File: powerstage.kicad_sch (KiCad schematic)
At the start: 0 parts

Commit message: Added driver and powerstage
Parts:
- added C10, C11, C12: 470uF, Capacitor_THT:CP_Radial_D17.0mm_P7.50mm, symbol Device:C_Polarized
- added C13, C14: 1uF, Capacitor_SMD:C_0805_2012Metric_Pad1.18x1.45mm_HandSolder, symbol Device:C
- added D10, D5, D6, D7, D8, D9: D_Zener, symbol Device:D_Zener
- added D2: B120-E3, Diode_SMD:D_SOD-128, symbol Diode:B120-E3
- added F1: Fuse, Fuse:Fuseholder_Cylinder-6.3x32mm_Schurter_0031-8002_Horizontal_Open, symbol Device:Fuse
- added H1: V_RAW, MountingHole:MountingHole_5.3mm_M5_Pad_Via, symbol Mechanical:MountingHole_Pad
- added H2: GND, MountingHole:MountingHole_5.3mm_M5_Pad_Via, symbol Mechanical:MountingHole_Pad
- added H3: PAD_A, MountingHole:MountingHole_5.3mm_M5_Pad_Via, symbol Mechanical:MountingHole_Pad
- added H4: PAD_B, MountingHole:MountingHole_5.3mm_M5_Pad_Via, symbol Mechanical:MountingHole_Pad
- added H5: PAD_C, MountingHole:MountingHole_5.3mm_M5_Pad_Via, symbol Mechanical:MountingHole_Pad
- added Q1, Q2, Q3, Q4, Q5, Q6: BSP89, Package_TO_SOT_THT:TO-220-3_Horizontal_TabDown, symbol Transistor_FET:BSP89
- added R10: 2k2, Resistor_SMD:R_1206_3216Metric, symbol Device:R
- added R11, R12, R13, R14, R15, R16, R17, R18, R19, R20, R21, R22: 10k, Resistor_SMD:R_1206_3216Metric, symbol Device:R
- added R9: 47k, Resistor_SMD:R_1206_3216Metric, symbol Device:R
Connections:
- new net: Q3.1 (G), R13.2, R19.2
- new net: Q2.1 (G), R12.2, R18.2
- new net: Q1.1 (G), R11.2, R17.2
- new net: F1.1, H1.1
- new net: Q6.1 (G), R16.2, R22.2
- new net: Q4.1 (G), R14.2, R20.2
- new net: Q5.1 (G), R15.2, R21.2
- new net COM_A: D5.2 (A), H3.1, Q1.3 (S), Q2.2 (D), R17.1
- new net COM_B: D7.2 (A), H4.1, Q3.3 (S), Q4.2 (D), R19.1
- new net COM_C: D9.2 (A), H5.1, Q5.3 (S), Q6.2 (D), R21.1
- new net DRV_AH: D5.1 (K), R11.1
- new net DRV_AL: D6.1 (K), R12.1
- new net DRV_BH: D7.1 (K), R13.1
- new net DRV_BL: D8.1 (K), R14.1
- new net DRV_CH: D9.1 (K), R15.1
- new net DRV_CL: D10.1 (K), R16.1
- new net GND: C10.2, C11.2, C12.2, C13.2, C14.2, D10.2 (A), D2.2 (A), D6.2 (A), D8.2 (A), H2.1, Q2.3 (S), Q4.3 (S), Q6.3 (S), R10.2, R18.1, R20.1, R22.1
- new net VSENSE: R10.1, R9.2
- new net V_RAW: C10.1, C11.1, C12.1, C13.1, C14.1, D2.1 (K), F1.2, Q1.2 (D), Q3.2 (D), Q5.2 (D), R9.1

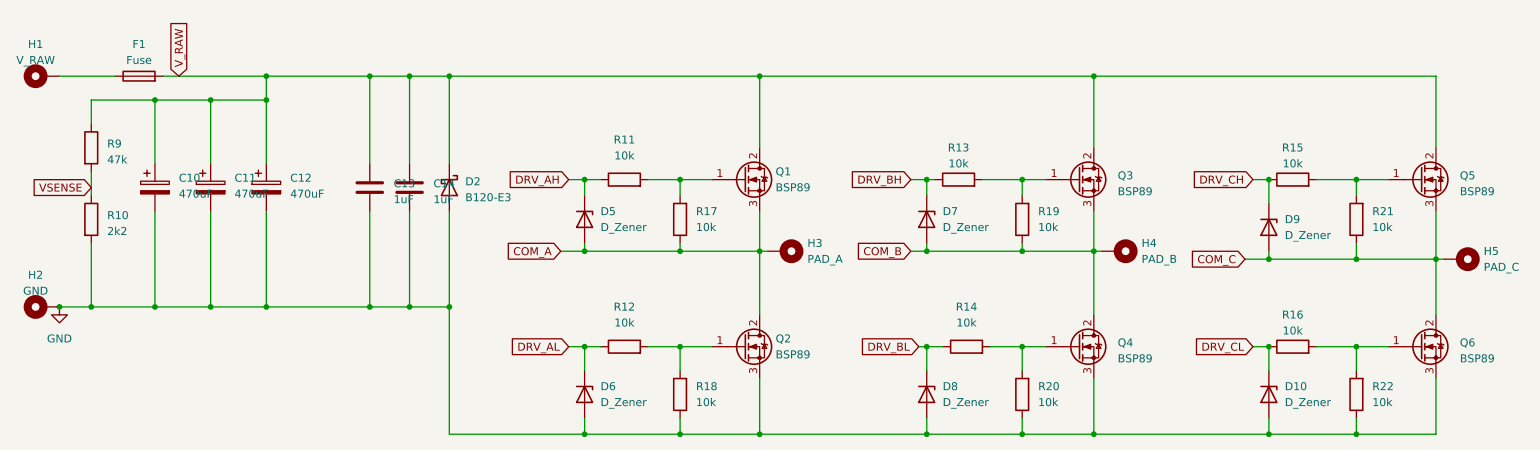
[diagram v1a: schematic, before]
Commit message: initial pcb placment, some components needs to be replaced by smd
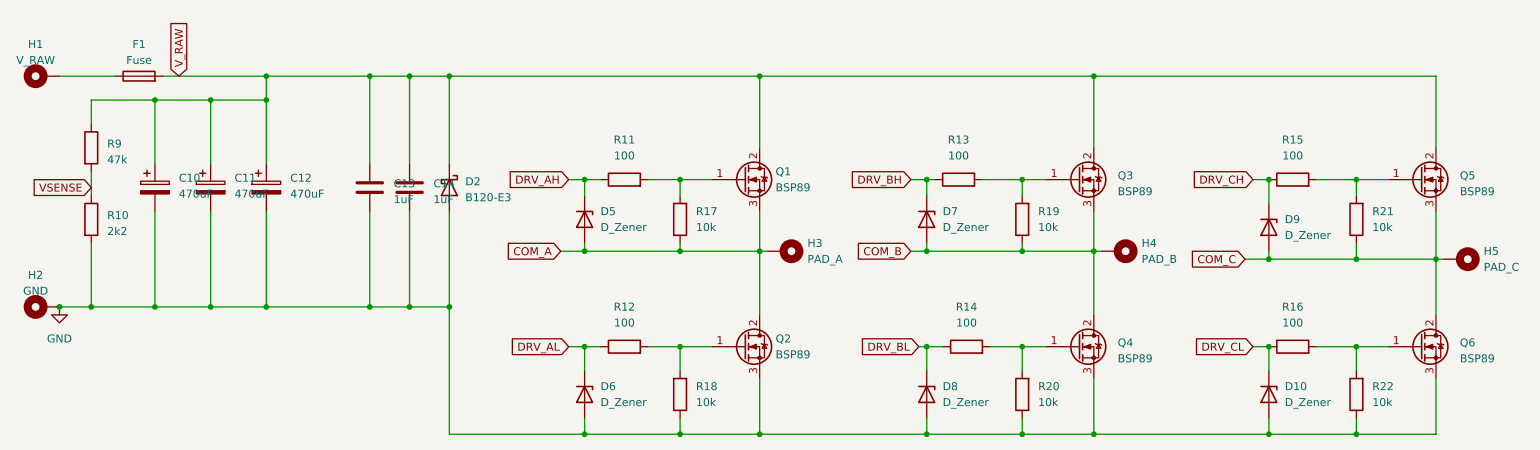
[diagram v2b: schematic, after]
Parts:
- C13, C14: footprint Capacitor_SMD:C_0805_2012Metric_Pad1.18x1.45mm_HandSolder -> Capacitor_THT:CP_Radial_Tantal_D5.5mm_P5.00mm
- D10, D5, D6, D7, D8, D9: footprint (none) -> Diode_THT:D_5W_P12.70mm_Horizontal
- D2: footprint Diode_SMD:D_SOD-128 -> Diode_THT:D_A-405_P10.16mm_Horizontal
- F1: footprint Fuse:Fuseholder_Cylinder-6.3x32mm_Schurter_0031-8002_Horizontal_Open -> Fuse:Fuse_Blade_ATO_directSolder
- H1, H2, H3, H4, H5: footprint MountingHole:MountingHole_5.3mm_M5_Pad_Via -> Connector_Wire:SolderWirePad_1x01_SMD_5x10mm
- Q1, Q2, Q3, Q4, Q5, Q6: footprint Package_TO_SOT_THT:TO-220-3_Horizontal_TabDown -> Package_TO_SOT_THT:TO-220-3_Vertical
- R10, R17, R18, R19, R20, R21, R22, R9: footprint Resistor_SMD:R_1206_3216Metric -> Resistor_THT:R_Axial_DIN0411_L9.9mm_D3.6mm_P15.24mm_Horizontal
- R11, R12, R13, R14, R15, R16: value 10k -> 100; footprint Resistor_SMD:R_1206_3216Metric -> Resistor_THT:R_Axial_DIN0411_L9.9mm_D3.6mm_P15.24mm_Horizontal

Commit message: Added first pcb design
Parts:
- added H6, H7, H8: V_RAW, Connector_Wire:SolderWirePad_1x01_SMD_5x10mm, symbol Mechanical:MountingHole_Pad
- C13, C14: footprint Capacitor_THT:CP_Radial_Tantal_D5.5mm_P5.00mm -> Capacitor_SMD:C_0805_2012Metric_Pad1.18x1.45mm_HandSolder
- Q1, Q2, Q3, Q4, Q5, Q6: footprint Package_TO_SOT_THT:TO-220-3_Vertical -> Package_TO_SOT_THT:TO-220-3_Horizontal_TabDown
- R10, R11, R12, R13, R14, R15, R16, R17, R18, R19, R20, R21, R22, R9: footprint Resistor_THT:R_Axial_DIN0411_L9.9mm_D3.6mm_P15.24mm_Horizontal -> Resistor_SMD:R_1206_3216Metric_Pad1.30x1.75mm_HandSolder
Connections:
- net V_RAW: now also H6.1, H7.1, H8.1
